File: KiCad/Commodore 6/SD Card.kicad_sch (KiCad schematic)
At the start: 1 part, among them J1 472192001

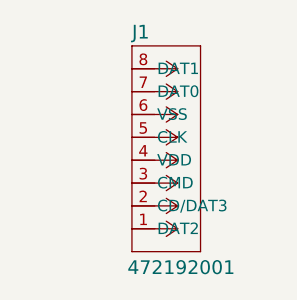
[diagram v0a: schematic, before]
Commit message: SD Card Routed
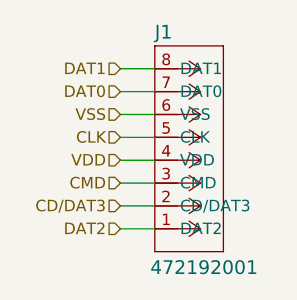
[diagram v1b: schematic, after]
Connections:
- net DAT2: now reaches J1.1 (DAT2)
- net CD/DAT3: now reaches J1.2 (CD/DAT3)
- net CMD: now reaches J1.3 (CMD)
- net VDD: now reaches J1.4 (VDD)
- net CLK: now reaches J1.5 (CLK)
- net VSS: now reaches J1.6 (VSS)
- net DAT0: now reaches J1.7 (DAT0)
- net DAT1: now reaches J1.8 (DAT1)
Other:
- moved on the sheet: J1
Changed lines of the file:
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@@
 	(generator_version "9.0")
 	(paper "A5")
+	(wire
+		(pts
+			(xy 99.06 53.34) (xy 102.87 53.34)
+		)
+		(stroke
+			(width 0)
+			(type default)
+		)
+	)
+	(wire
+		(pts
+			(xy 99.06 55.88) (xy 102.87 55.88)
+		)
+		(stroke
+			(width 0)
+			(type default)
+		)
+	)
+	(wire
+		(pts
+			(xy 99.06 63.5) (xy 102.87 63.5)
+		)
+		(stroke
+			(width 0)
+			(type default)
+		)
+	)
+	(wire
+		(pts
+			(xy 99.06 66.04) (xy 102.87 66.04)
+		)
+		(stroke
+			(width 0)
+			(type default)
+		)
+	)
+	(wire
+		(pts
+			(xy 99.06 71.12) (xy 102.87 71.12)
+		)
+		(stroke
+			(width 0)
+			(type default)
+		)
+	)
+	(wire
+		(pts
+			(xy 99.06 58.42) (xy 102.87 58.42)
+		)
+		(stroke
+			(width 0)
+			(type default)
+		)
+	)
+	(wire
+		(pts
+			(xy 99.06 68.58) (xy 102.87 68.58)
+		)
+		(stroke
+			(width 0)
+			(type default)
+		)
+	)
+	(wire
+		(pts
+			(xy 99.06 60.96) (xy 102.87 60.96)
+		)
+		(stroke
+			(width 0)
+			(type default)
+		)
+	)
+	(hierarchical_label "VSS"
+		(shape input)
+		(at 99.06 58.42 180)
+		(effects
+			(font
+				(size 1.27 1.27)
+			)
+			(justify right)
+		)
+	)
+	(hierarchical_label "CD{slash}DAT3"
+		(shape input)
+		(at 99.06 68.58 180)
+		(effects
+			(font
+				(size 1.27 1.27)
+			)
+			(justify right)
+		)
+	)
+	(hierarchical_label "DAT2"
+		(shape input)
+		(at 99.06 71.12 180)
+		(effects
+			(font
+				(size 1.27 1.27)
+			)
+			(justify right)
+		)
+	)
+	(hierarchical_label "CMD"
+		(shape input)
+		(at 99.06 66.04 180)
+		(effects
+			(font
+				(size 1.27 1.27)
+			)
+			(justify right)
+		)
+	)
+	(hierarchical_label "DAT0"
+		(shape input)
+		(at 99.06 55.88 180)
+		(effects
+			(font
+				(size 1.27 1.27)
+			)
+			(justify right)
+		)
+	)
+	(hierarchical_label "DAT1"
+		(shape input)
+		(at 99.06 53.34 180)
+		(effects
+			(font
+				(size 1.27 1.27)
+			)
+			(justify right)
+		)
+	)
+	(hierarchical_label "VDD"
+		(shape input)
+		(at 99.06 63.5 180)
+		(effects
+			(font
+				(size 1.27 1.27)
+			)
+			(justify right)
+		)
+	)
+	(hierarchical_label "CLK"
+		(shape input)
+		(at 99.06 60.96 180)
+		(effects
+			(font
+				(size 1.27 1.27)
+			)
+			(justify right)
+		)
+	)
 	(symbol
 		(lib_id "472192001 Micro SD Card:472192001")
-		(at 95.25 53.34 0)
+		(at 97.79 53.34 0)
 		(unit 1)
 		(exclude_from_sim no)
@@
 		(dnp no)
 		(property "Reference" "J1"
-			(at 100.33 49.276 0)
+			(at 102.87 49.276 0)
 			(effects
 				(font
@@
 		)
 		(property "Value" "472192001"
-			(at 99.822 75.438 0)
+			(at 102.362 75.438 0)
 			(effects
 				(font
@@
 		)
 		(property "Footprint" "Connector_Card:microSD_HC_Molex_47219-2001"
-			(at 122.428 77.724 0)
+			(at 124.968 77.724 0)
 			(effects
 				(font
@@
 		)
 		(property "Datasheet" "https://www.molex.com/en-us/products/part-detail-pdf/472192001?display=pdf"
-			(at 139.7 75.184 0)
+			(at 142.24 75.184 0)
 			(effects
 				(font
@@
 		)
 		(property "Description" ""
-			(at 95.25 53.34 0)
+			(at 97.79 53.34 0)
 			(effects
 				(font
@@
 		)
 		(instances
-			(project ""
-				(path "/27ad1105-577c-4f6a-be9a-9e41c9021a88/a17d9f5b-72ac-4087-9da9-426ded6802ea"
+			(project "Commodore 6"
+				(path "/27ad1105-577c-4f6a-be9a-9e41c9021a88/42b4c9db-c3d3-48b6-9c84-e282be31bb83/3b4ad586-1ff1-4a88-afa6-15c3dc9fb0f6"
 					(reference "J1")
 					(unit 1)
